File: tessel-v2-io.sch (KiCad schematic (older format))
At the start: 73 parts, among them J801 USB-micro-TH, J802 CONN_01X07, J803 HR911105A, J806 CONN_01X02, J807 CONN_01X02, J809 USB_A_2_stack, J810 MODULE_HEADER, J811 USB_A_2_stack, J813 MODULE_HEADER, J814 CONN_02X05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

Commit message: usb esd
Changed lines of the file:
@@
 Connection ~ 2650 8750
 Wire Wire Line
-	2650 8750 2650 9450
+	2650 8750 2650 9550
 Wire Wire Line
 	2150 8750 3200 8750
@@
 Wire Wire Line
 	9900 6550 10000 6550
-Wire Wire Line
-	2650 9450 2850 9450
-Wire Wire Line
-	2850 9550 2750 9550
-Wire Wire Line
-	2750 9550 2750 8850
 Connection ~ 2750 8850
 Wire Wire Line
@@
 Wire Wire Line
 	3700 7250 4400 7250
+Wire Wire Line
+	2650 9550 2850 9550
+Wire Wire Line
+	2850 9450 2750 9450
+Wire Wire Line
+	2750 9450 2750 8850
 $EndSCHEMATC

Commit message: post-schematic review. changes in.
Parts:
- added C803: 10uF DNP, SMD_Packages:SMD-0805, symbol C
- added R827: 22R, tm-kicad-lib:SMD-0402, symbol R
- added R828: 1R DNP, SMD_Packages:SMD-0603, symbol R
- added R829: 100kR, tm-kicad-lib:SMD-0402, symbol R
- C818: value 0.1uF -> 100nF
- J817: footprint Pin_Headers:Pin_Header_Straight_1x01 -> !Parts:Testpoint
- R802: value 4.7kR -> 100kR
- R806, R810: value 4.7kR -> 1kR
- R811, R812, R813, R814: value DNP -> 10kR DNP
- R820, R821: value 22R -> 330R
- R822, R823: value 300R -> 330R
- R825, R826: value DNP -> 100kR DNP
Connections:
- net labels added: MT_GPIO_HOLD, MT_GPIO_WP, VBUS[1]_IN, VBUS[2]_IN, VBUS[3]_IN, VBUS[4]_IN
- net labels removed: MT_SPI_HOLD, MT_WP
- wire segments 364 -> 371
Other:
- note added: "POWER DETECTION =\nMEDIATEK POWERED?"

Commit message: added esd/gnd loop deterrent to sockets
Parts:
- added C? (x4): 100pF, tm-kicad-lib:SMD-0402, symbol C
- added R? (x4): 100kR, tm-kicad-lib:SMD-0402, symbol R
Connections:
- wire segments 371 -> 502

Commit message: stupid thing did not annotate properly
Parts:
- gave numbers to parts that had none: 8
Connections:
- wire segments 502 -> 394

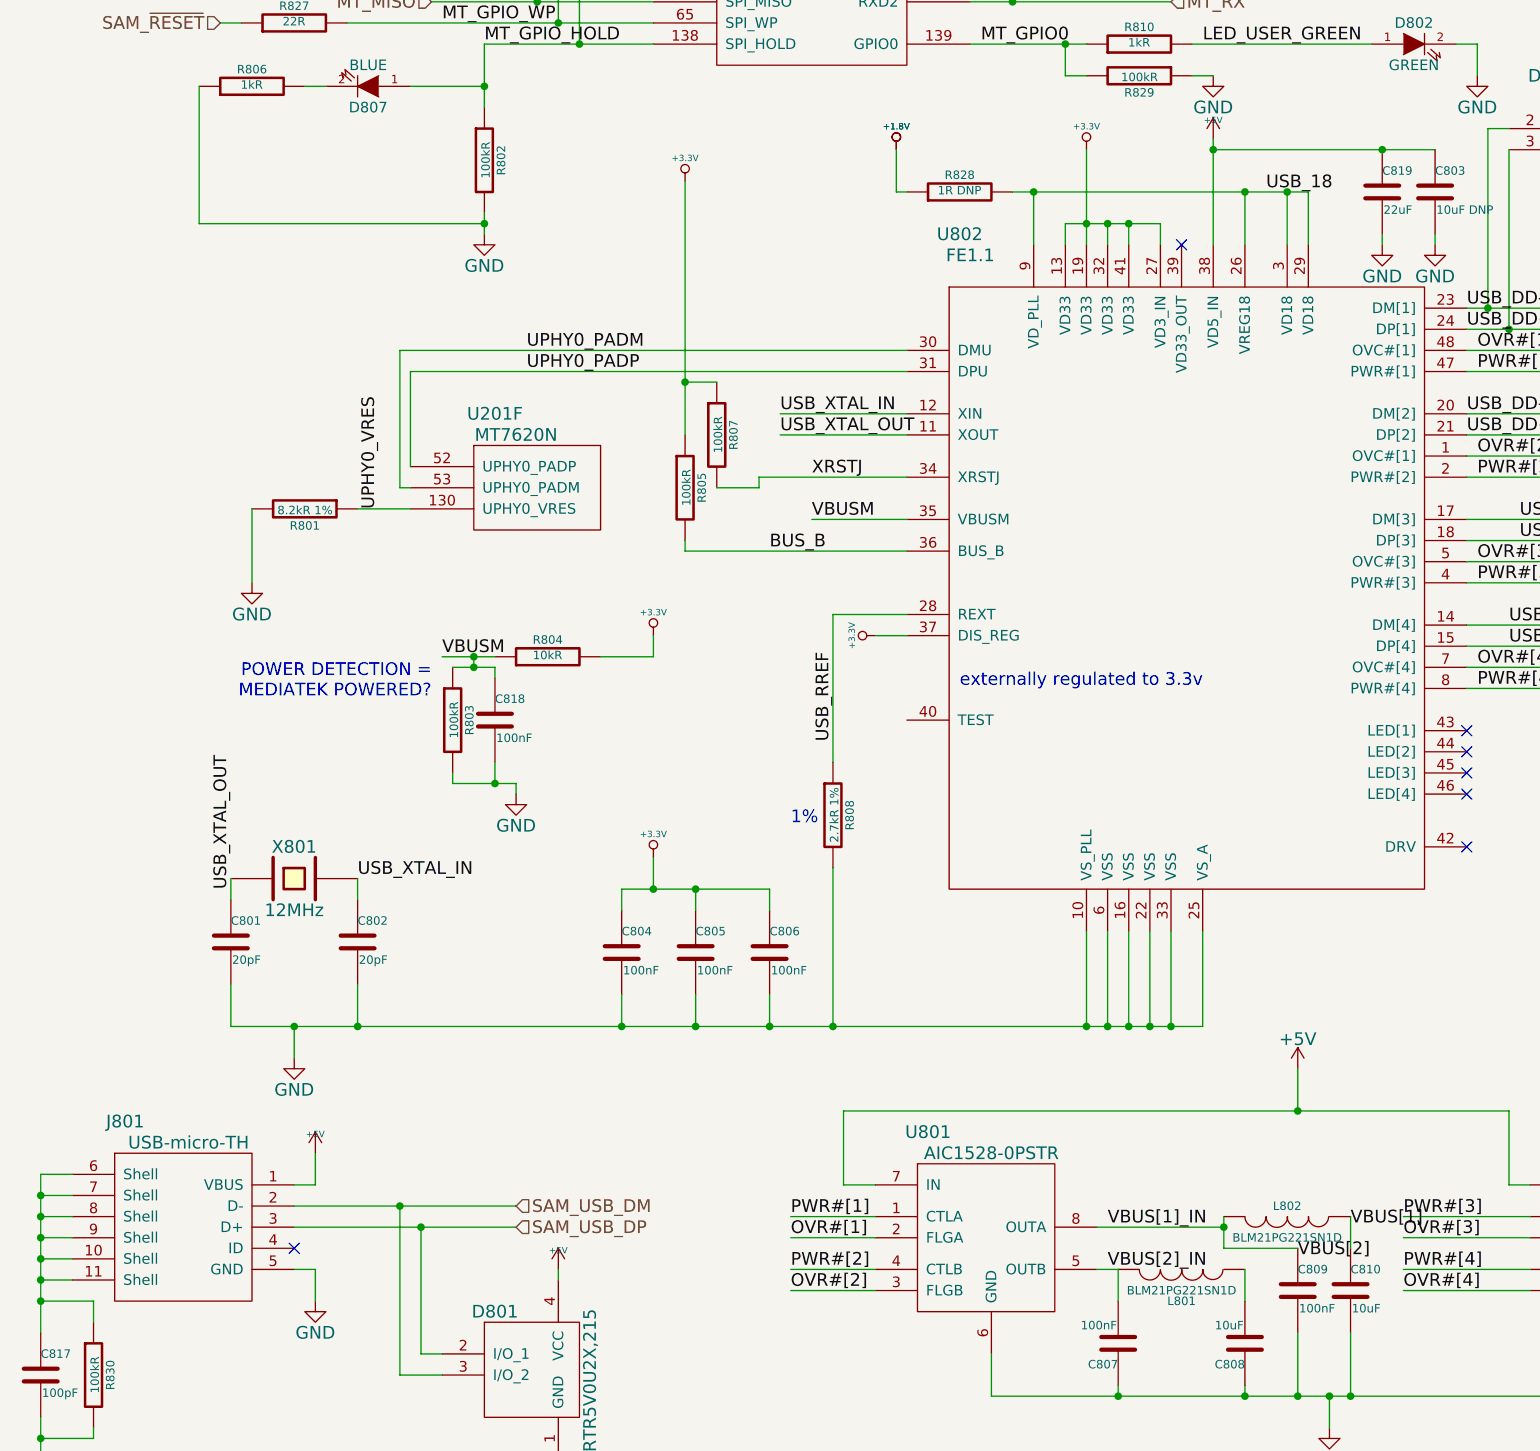
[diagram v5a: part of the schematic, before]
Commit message: derating load caps
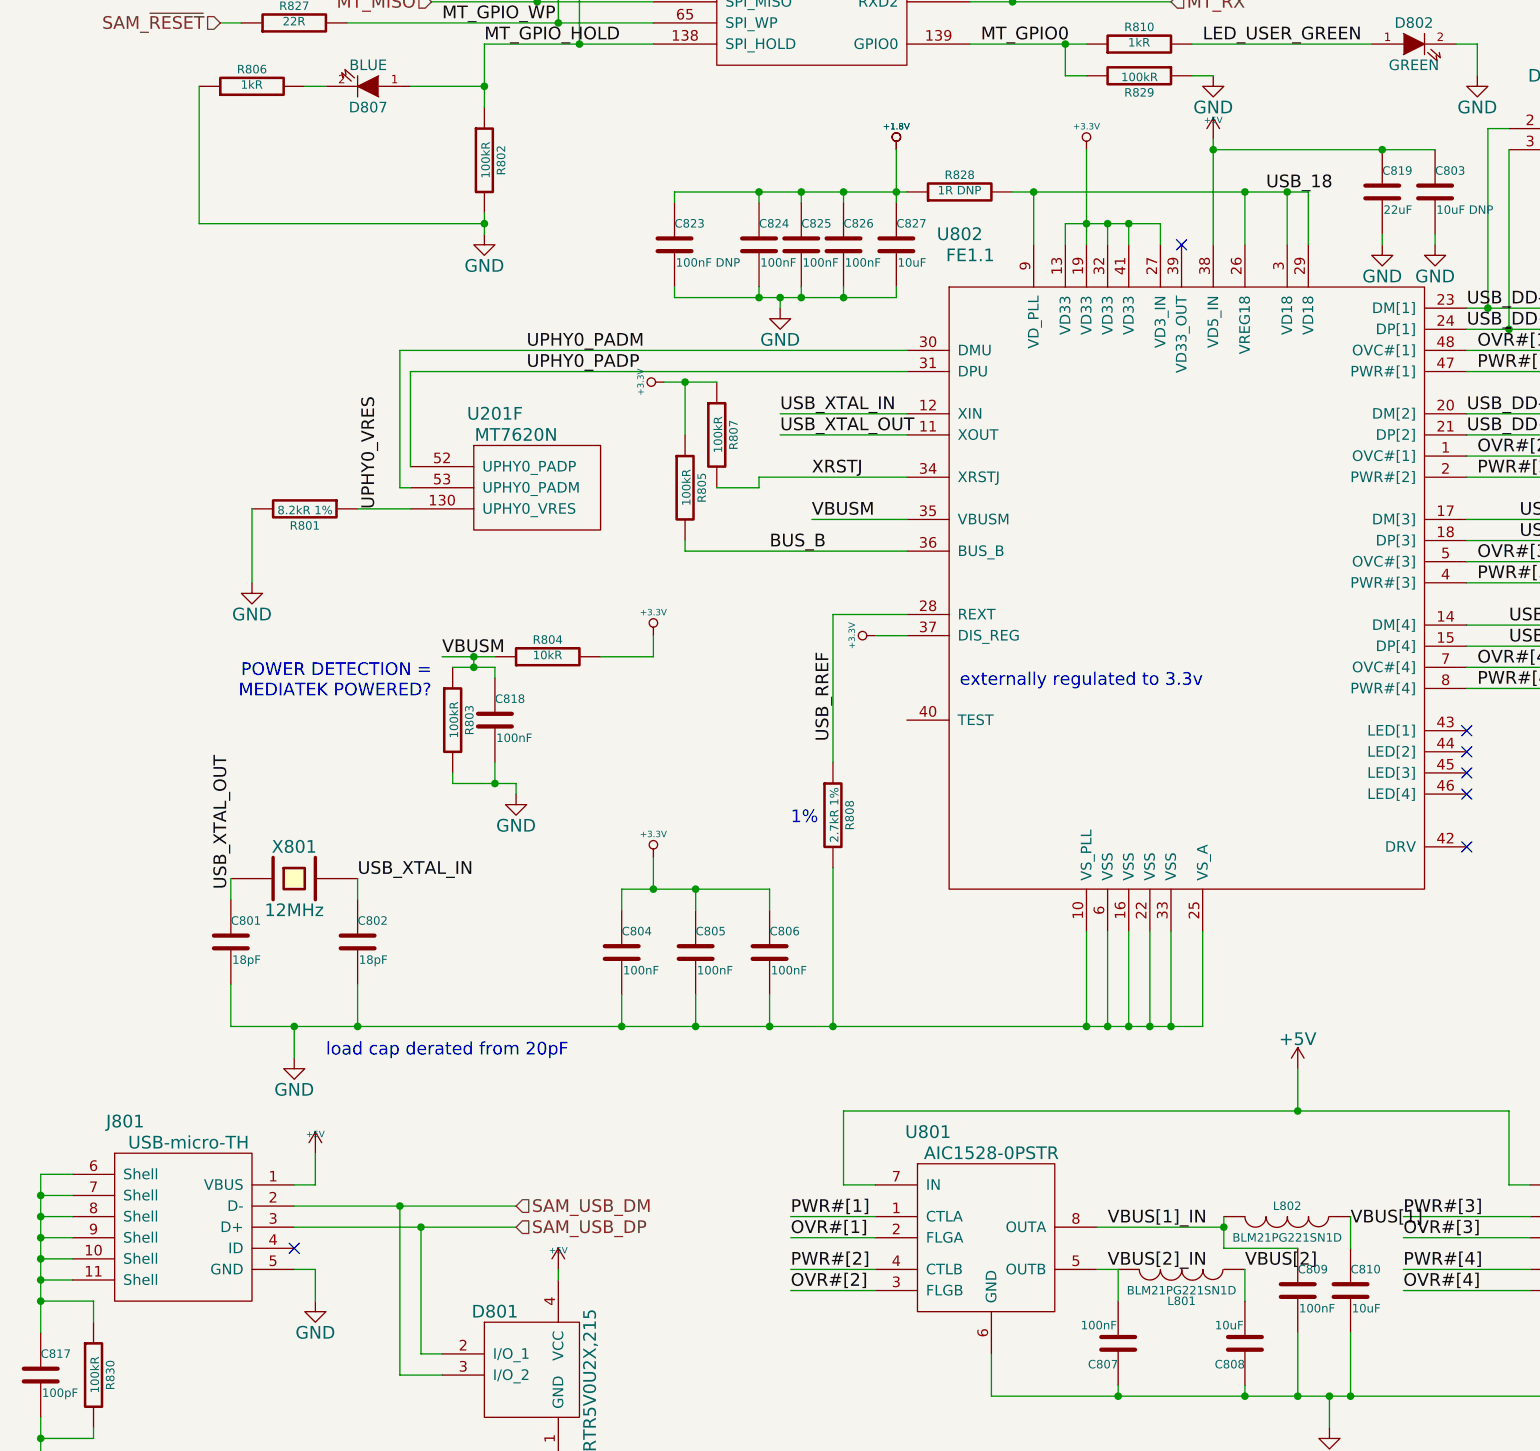
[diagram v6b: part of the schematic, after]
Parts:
- added C823: 100nF DNP, tm-kicad-lib:SMD-0402, symbol C
- added C824, C825, C826: 100nF, tm-kicad-lib:SMD-0402, symbol C
- added C827: 10uF, SMD_Packages:SMD-0805, symbol C
- C801, C802: value 20pF -> 18pF
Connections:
- wire segments 394 -> 405
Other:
- note added: "load cap derated from 20pF"
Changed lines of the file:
@@
 P 1850 7500
 F 0 "C801" H 1850 7600 40  0000 L CNN
-F 1 "20pF" H 1856 7415 40  0000 L CNN
+F 1 "18pF" H 1856 7415 40  0000 L CNN
 F 2 "tm-kicad-lib:SMD-0402" H 1888 7350 30  0001 C CNN
 F 3 "" H 1850 7500 60  0000 C CNN
@@
 P 2450 7500
 F 0 "C802" H 2450 7600 40  0000 L CNN
-F 1 "20pF" H 2456 7415 40  0000 L CNN
+F 1 "18pF" H 2456 7415 40  0000 L CNN
 F 2 "tm-kicad-lib:SMD-0402" H 2488 7350 30  0001 C CNN
 F 3 "" H 2450 7500 60  0000 C CNN
@@
 L +3.3V #PWR0127
 U 1 1 5495DD22
-P 4000 3900
-F 0 "#PWR0127" H 4000 3860 30  0001 C CNN
-F 1 "+3.3V" H 4000 4010 30  0000 C CNN
-F 2 "" H 4000 3900 60  0000 C CNN
-F 3 "" H 4000 3900 60  0000 C CNN
-	1    4000 3900
-	1    0    0    -1
+P 3900 4850
+F 0 "#PWR0127" H 3900 4810 30  0001 C CNN
+F 1 "+3.3V" H 3900 4960 30  0000 C CNN
+F 2 "" H 3900 4850 60  0000 C CNN
+F 3 "" H 3900 4850 60  0000 C CNN
+	1    3900 4850
+	0    -1   1    0
 $EndComp
 $Comp
@@
 Connection ~ 4000 4850
 Wire Wire Line
-	4000 4850 4150 4850
+	3900 4850 4150 4850
 Connection ~ 5550 3050
 Wire Wire Line
@@
 Wire Wire Line
 	4700 7900 4700 7150
-Wire Wire Line
-	4000 3900 4000 5100
 Wire Wire Line
 	7700 4800 8150 4800
@@
 Connection ~ 5650 3950
 Wire Wire Line
-	5000 3950 5050 3950
-Wire Wire Line
-	5000 3750 5000 3950
+	3950 3950 5050 3950
+Wire Wire Line
+	5000 3750 5000 4000
 Text Label 7150 8850 0    60   ~ 0
 VBUS[1]
-Text Label 6900 9000 0    60   ~ 0
+Text Label 6650 9050 0    60   ~ 0
 VBUS[2]
 Text Label 9100 9050 0    60   ~ 0
@@
 	1200 9300 1200 9200
 Wire Wire Line
-	950  9200 1200 9200
+	1200 9200 950  9200
 Wire Wire Line
 	950  8600 950  9350
@@
 	11200 3750 11200 3850
 Connection ~ 11300 3750
+$Comp
+L C C827
+U 1 1 54C72287
+P 5000 4200
+F 0 "C827" H 5000 4300 40  0000 L CNN
+F 1 "10uF" H 5006 4115 40  0000 L CNN
+F 2 "SMD_Packages:SMD-0805" H 5038 4050 30  0001 C CNN
+F 3 "" H 5000 4200 60  0000 C CNN
+	1    5000 4200
+	1    0    0    -1
+$EndComp
+$Comp
+L C C826
+U 1 1 54C7260B
+P 4750 4200
+F 0 "C826" H 4750 4300 40  0000 L CNN
+F 1 "100nF" H 4756 4115 40  0000 L CNN
+F 2 "tm-kicad-lib:SMD-0402" H 4788 4050 30  0001 C CNN
+F 3 "" H 4750 4200 60  0000 C CNN
+	1    4750 4200
+	1    0    0    -1
+$EndComp
+$Comp
+L C C825
+U 1 1 54C728F6
+P 4550 4200
+F 0 "C825" H 4550 4300 40  0000 L CNN
+F 1 "100nF" H 4556 4115 40  0000 L CNN
+F 2 "tm-kicad-lib:SMD-0402" H 4588 4050 30  0001 C CNN
+F 3 "" H 4550 4200 60  0000 C CNN
+	1    4550 4200
+	1    0    0    -1
+$EndComp
+$Comp
+L C C824
+U 1 1 54C72972
+P 4350 4200
+F 0 "C824" H 4350 4300 40  0000 L CNN
+F 1 "100nF" H 4356 4115 40  0000 L CNN
+F 2 "tm-kicad-lib:SMD-0402" H 4388 4050 30  0001 C CNN
+F 3 "" H 4350 4200 60  0000 C CNN
+	1    4350 4200
+	1    0    0    -1
+$EndComp
+$Comp
+L C C823
+U 1 1 54C729ED
+P 3950 4200
+F 0 "C823" H 3950 4300 40  0000 L CNN
+F 1 "100nF DNP" H 3956 4115 40  0000 L CNN
+F 2 "tm-kicad-lib:SMD-0402" H 3988 4050 30  0001 C CNN
+F 3 "" H 3950 4200 60  0000 C CNN
+	1    3950 4200
+	1    0    0    -1
+$EndComp
+Wire Wire Line
+	4000 4850 4000 5100
+Wire Wire Line
+	4750 3950 4750 4000
+Connection ~ 5000 3950
+Wire Wire Line
+	4550 3950 4550 4000
+Connection ~ 4750 3950
+Wire Wire Line
+	4350 3950 4350 4000
+Connection ~ 4550 3950
+Wire Wire Line
+	3950 3950 3950 4000
+Connection ~ 4350 3950
+Wire Wire Line
+	3950 4400 3950 4450
+Wire Wire Line
+	3950 4450 5000 4450
+Wire Wire Line
+	4350 4450 4350 4400
+Wire Wire Line
+	4550 4450 4550 4400
+Connection ~ 4350 4450
+Wire Wire Line
+	4750 4450 4750 4400
+Connection ~ 4550 4450
+Wire Wire Line
+	5000 4450 5000 4400
+Connection ~ 4750 4450
+$Comp
+L GND #PWR0165
+U 1 1 54C7542F
+P 4450 4500
+F 0 "#PWR0165" H 4450 4250 60  0001 C CNN
+F 1 "GND" H 4450 4350 60  0000 C CNN
+F 2 "" H 4450 4500 60  0000 C CNN
+F 3 "" H 4450 4500 60  0000 C CNN
+	1    4450 4500
+	1    0    0    -1
+$EndComp
+Wire Wire Line
+	4450 4500 4450 4450
+Connection ~ 4450 4450
+Text Notes 2300 8050 0    60   ~ 0
+load cap derated from 20pF
 $EndSCHEMATC

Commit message: swapped down to a 4-pin "gpio bank"
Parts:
- removed J818: CONN_01X08, Pin_Headers:Pin_Header_Straight_1x08, symbol CONN_01X08
- added J?: CONN_01X04, symbol CONN_01X04
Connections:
- wire segments 405 -> 517

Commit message: fixed usb1.8v, routed esd
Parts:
- C819: footprint Capacitors_SMD:C_0805 -> SMD_Packages:SMD-0805
- J804: renamed from J?; footprint (none) -> Pin_Headers:Pin_Header_Straight_1x04
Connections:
- wire segments 517 -> 402
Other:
- moved on the sheet: R828
